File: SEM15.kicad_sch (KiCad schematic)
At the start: 47 parts, among them Q1 PMOS, Q2 PMOS, Q3 PMOS, Q4 PMOS, Q5 PMOS, Q6 PMOS

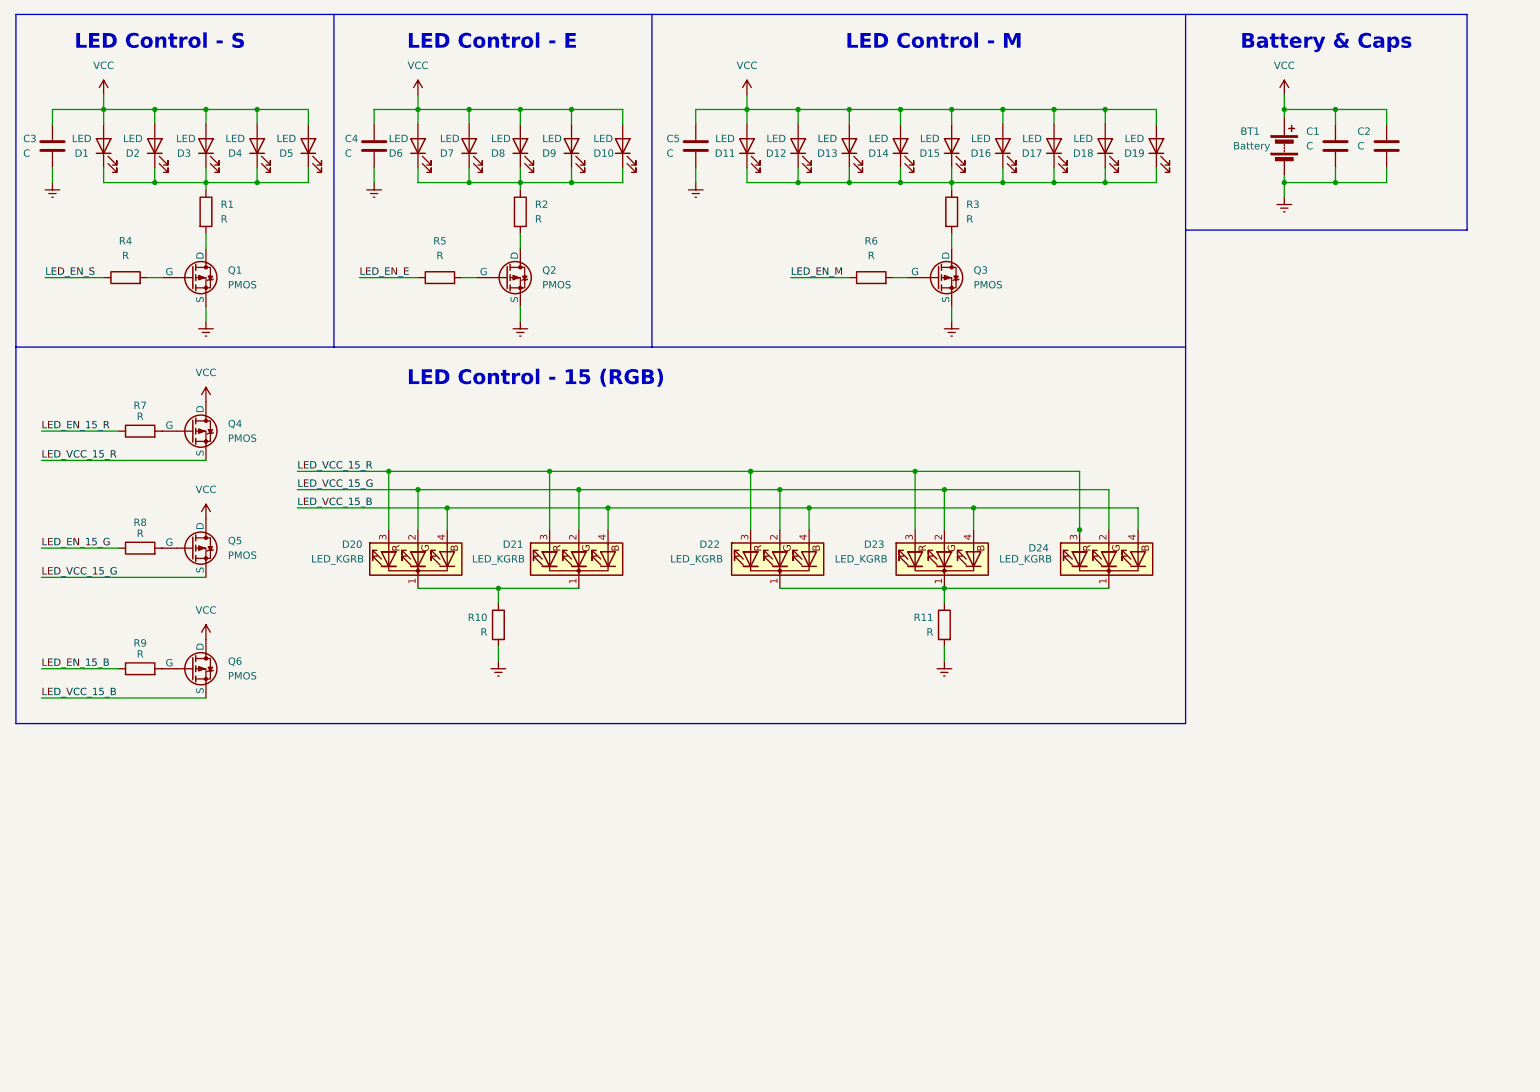
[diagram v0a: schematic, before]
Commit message: rgb es feher led meghajtasa, mikrovezerlo, pcb-n alkatreszrendezgets
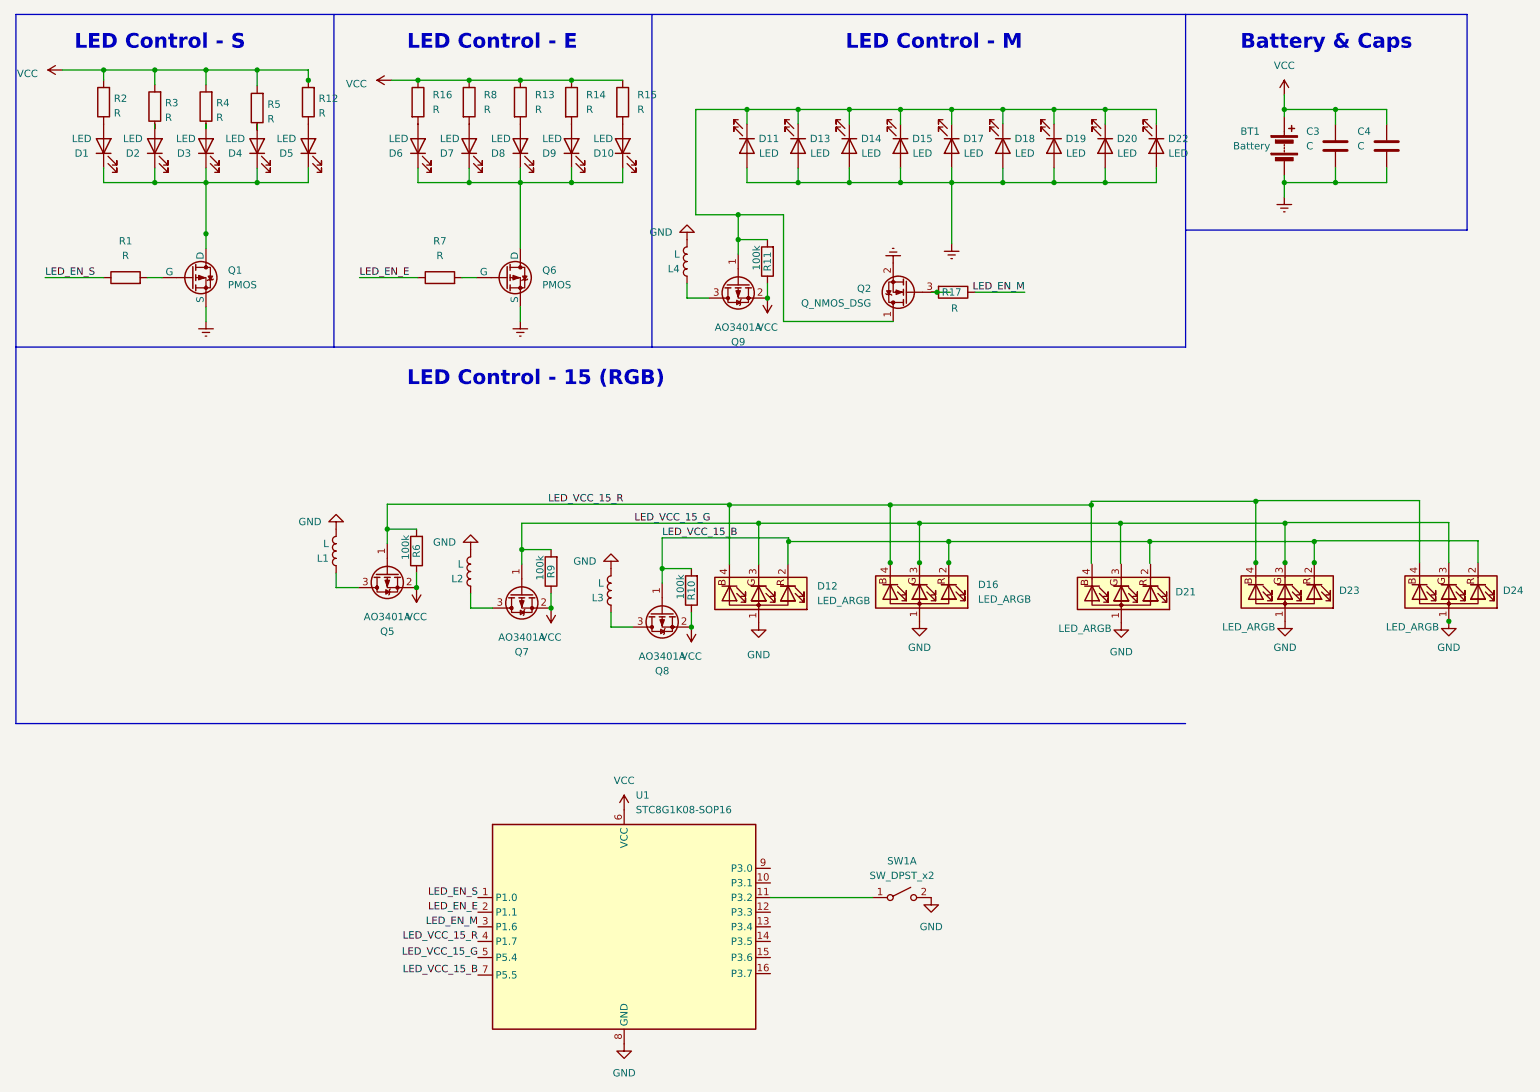
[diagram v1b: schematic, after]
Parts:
- removed C3, C4, C5: C, symbol Device:C
- removed D20, D21, D22, D23, D24: LED_KGRB, LED_SMD:LED_Cree-PLCC4_2x2mm_CW, symbol Device:LED_KGRB
- removed Q3, Q4, Q5, Q6: PMOS, symbol Simulation_SPICE:PMOS
- removed R1, R7: R, symbol Device:R
- added D12, D16, D21, D23, D24: LED_ARGB, LED_SMD:LED_RGB_Wuerth-PLCC4_3.2x2.8mm_150141M173100, symbol Device:LED_ARGB
- added L1, L2, L3, L4: L, Inductor_SMD:L_1008_2520Metric, symbol Device:L
- added Q2: Q_NMOS_DSG, symbol Device:Q_NMOS_DSG
- added Q5, Q7, Q8, Q9: AO3401A, sajat:SOT-23, symbol Transistor_FET:AO3401A
- added R12, R13, R14, R15, R16, R17, R4, R5: R, Resistor_SMD:R_0603_1608Metric, symbol Device:R
- added SW1: SW_DPST_x2, sajat:SW_Push_K2-1102SP, symbol Switch:SW_DPST_x2
- added U1: STC8G1K08-SOP16, Package_SO:STC_SOP-16_3.9x9.9mm_P1.27mm, symbol karifa:STC8G1K08-SOP16
- BT1: footprint (none) -> karifa:CR2032_Holder
- C3: renamed from C1; footprint (none) -> Capacitor_SMD:C_0805_2012Metric
- C4: renamed from C2; footprint (none) -> Capacitor_SMD:C_0805_2012Metric
- R1: renamed from R4; footprint (none) -> Resistor_SMD:R_0603_1608Metric
- R10, R11, R6, R9: value R -> 100k; footprint (none) -> Resistor_SMD:R_0603_1608Metric
- R2, R3, R8: footprint (none) -> Resistor_SMD:R_0603_1608Metric
- R7: renamed from R5; footprint (none) -> Resistor_SMD:R_0603_1608Metric
- renumbered D12 to D13, D13 to D14, D14 to D15, D15 to D17, D16 to D18, D17 to D19, D18 to D20, D19 to D22, Q2 to Q6
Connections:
- net LED_EN_15_B is gone; now on net VCC: R9.1
- net LED_EN_15_G is gone; now on net VCC: R8.1
- net Earth: now also D11.2 (A), D13.2 (A), D14.2 (A), D15.2 (A), D17.2 (A), D18.2 (A), D19.2 (A), D20.2 (A), D22.2 (A), Q2.2 (S); no longer R10.2, R11.2
- net LED_EN_E: now also U1.2 (P1.1)
- net LED_EN_M: now also R17.1, U1.3 (P1.6); no longer R6.1
- net LED_EN_S: now also U1.1 (P1.0)
- net LED_VCC_15_B: now also R10.2, D12.2 (RK), D16.2 (RK), D23.2 (RK), D24.2 (RK), Q8.1 (G), U1.7 (P5.5)
- net LED_VCC_15_G: now also R9.2, D12.3 (GK), D16.3 (GK), D23.3 (GK), D24.3 (GK), Q7.1 (G), U1.5 (P5.4)
- net LED_VCC_15_R: now also R6.2, D12.4 (BK), D16.4 (BK), D23.4 (BK), D24.4 (BK), Q5.1 (G), U1.4 (P1.7)
- net VCC: now also R10.1, R11.1, R2.2, R3.2, R6.1, Q5.2 (S), Q7.2 (S), Q8.2 (S), Q9.2 (S), R12.2, R13.1, R14.1, R15.1, R16.1, R4.2, R5.2, U1.6 (VCC); no longer D1.2 (A), D10.2 (A), D11.2 (A), D13.2 (A), D14.2 (A), D15.2 (A), D17.2 (A), D18.2 (A), D19.2 (A), D2.2 (A), D20.2 (A), D22.2 (A), D3.2 (A), D4.2 (A), D5.2 (A), D6.2 (A), D7.2 (A), D8.2 (A), D9.2 (A)
- net at D11.1 (K), D13.1 (K), D14.1 (K)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: now also R11.2, Q2.1 (D), Q9.1 (G); no longer R3.1
- net at D1.1 (K), D2.1 (K), D3.1 (K)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: now also Q1.1 (D)
- net at D10.1 (K), D6.1 (K), D7.1 (K)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: now also Q6.1 (D); no longer R2.1
- net at R8.2: now also D7.2 (A)
- new net: D10.2 (A), R15.2
- new net: L4.1, Q9.3 (D)
- new net: L1.1, Q5.3 (D)
- new net: D3.2 (A), R4.1
- new net: D1.2 (A), R2.1
- new net: L3.1, Q8.3 (D)
- new net: D4.2 (A), R5.1
- new net: D9.2 (A), R14.2
- new net: SW1.1 (A), U1.11 (P3.2)
- new net: Q2.3 (G), R17.2
- new net: D6.2 (A), R16.2
- new net: L2.1, Q7.3 (D)
- new net: D2.2 (A), R3.1
- new net: D8.2 (A), R13.2
- new net: D5.2 (A), R12.1
- new net GND: D12.1 (A), D16.1 (A), D21.1 (A), D23.1 (A), D24.1 (A), L1.2, L2.2, L3.2, L4.2, SW1.2 (B), U1.8 (GND)
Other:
- moved on the sheet: D11, D13, D14, D15, D17, D18, D19, D20, D22

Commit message: sch kesz
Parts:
- removed D12, D16, D21, D23, D24: LED_ARGB, LED_SMD:LED_RGB_Wuerth-PLCC4_3.2x2.8mm_150141M173100, symbol Device:LED_ARGB
- removed L3: L, Inductor_SMD:L_1008_2520Metric, symbol Device:L
- removed Q1, Q6: PMOS, symbol Simulation_SPICE:PMOS
- removed Q2: Q_NMOS_DSG, symbol Device:Q_NMOS_DSG
- removed Q5, Q7, Q8, Q9: AO3401A, sajat:SOT-23, symbol Transistor_FET:AO3401A
- removed R10: 100k, Resistor_SMD:R_0603_1608Metric, symbol Device:R
- removed R13, R14, R15, R16, R17: R, Resistor_SMD:R_0603_1608Metric, symbol Device:R
- added D12, D16, D21, D25, D26, D27, D28, D29: LED, LED_SMD:LED_0805_2012Metric, symbol Device:LED
- added J1: Conn_01x04, Connector_PinHeader_1.27mm:PinHeader_1x04_P1.27mm_Vertical, symbol Connector_Generic:Conn_01x04
- added L5: L, Inductor_SMD:L_1008_2520Metric, symbol Device:L
- added Q1, Q2, Q3, Q4: AO3401A, sajat:SOT-23, symbol Transistor_FET:AO3401A
- R1: value R -> 100k
- R12, R4, R5, R7, R8: footprint Resistor_SMD:R_0603_1608Metric -> (none)
- R2: value R -> 510; footprint Resistor_SMD:R_0603_1608Metric -> (none)
- R3: value R -> 1k; footprint Resistor_SMD:R_0603_1608Metric -> (none)
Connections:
- net Earth: now also D1.2 (A), D10.2 (A), D2.2 (A), D3.2 (A), D4.2 (A), D5.2 (A), D6.2 (A), D7.2 (A), D8.2 (A), D9.2 (A), D25.2 (A), D26.2 (A), D27.2 (A), D28.2 (A), D29.2 (A); no longer D11.2 (A), D13.2 (A), D14.2 (A), D15.2 (A), D17.2 (A), D18.2 (A), D19.2 (A), D20.2 (A), D22.2 (A)
- net GND: now also J1.4 (Pin_4), L5.2
- net LED_EN_E: now also R1.2, Q2.1 (G); no longer R7.1
- net LED_EN_M: no longer U1.3 (P1.6)
- net LED_EN_S: now also R11.2, Q1.1 (G); no longer R1.1
- net VCC: now also R1.1, R7.2, R8.2, J1.1 (Pin_1), Q1.2 (S), Q2.2 (S), Q3.2 (S), Q4.2 (S); no longer R8.1
- net at L4.1: now also D1.1 (K), D2.1 (K), D3.1 (K), D4.1 (K), D5.1 (K), Q1.3 (D)
- net at L1.1: now also D12.1 (K), D16.1 (K), D21.1 (K), Q3.3 (D)
- net at R4.1: now also D15.2 (A); no longer D3.2 (A)
- net at R2.1: now also D11.2 (A), D13.2 (A); no longer D1.2 (A)
- net at R5.1: now also D17.2 (A); no longer D4.2 (A)
- net P3.1: now reaches U1.10 (P3.1)
- net P3.1: now also J1.3 (Pin_3)
- net LED_EN_M5: now reaches U1.12 (P3.3)
- net LED_EN_M5: now also D18.1 (K)
- net LED_EN_M6: now reaches U1.13 (P3.4)
- net LED_EN_M6: now also D19.1 (K)
- net LED_EN_M7: now reaches U1.14 (P3.5)
- net LED_EN_M7: now also D20.1 (K), D22.1 (K)
- net LED_EN_1: now reaches U1.15 (P3.6)
- net LED_EN_1: now also R6.2, Q3.1 (G)
- net LED_EN_5: now reaches U1.16 (P3.7)
- net LED_EN_5: now also R9.2, Q4.1 (G)
- net P3.0: now reaches U1.9 (P3.0)
- net P3.0: now also J1.2 (Pin_2)
- net at L2.1: now also D25.1 (K), D26.1 (K), D27.1 (K), D28.1 (K), D29.1 (K), Q4.3 (D)
- net at R3.1: now also D14.2 (A); no longer D2.2 (A)
- net at R12.1: now also D20.2 (A), D22.2 (A); no longer D5.2 (A)
- net LED_VCC_15_B renamed LED_EN_M4
- net LED_EN_M4: now also D17.1 (K)
- net LED_VCC_15_G renamed LED_EN_M3
- net LED_EN_M3: now also D15.1 (K); no longer R9.2
- net LED_VCC_15_R renamed LED_EN_M2
- net LED_EN_M2: now also D14.1 (K); no longer R6.2
- new net: L5.1, Q2.3 (D)
- new net: D18.2 (A), R7.1
- new net: D19.2 (A), R8.1
- new net: D12.2 (A), D16.2 (A), D21.2 (A)
- new net LED_EN_M1: D11.1 (K), D13.1 (K), U1.3 (P1.6)
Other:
- moved on the sheet: D1, D10, D2, D3, D4, D5, D6, D7, D8, D9

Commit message: pcb nagyreszt
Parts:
- removed D16: LED, LED_SMD:LED_0805_2012Metric, symbol Device:LED
- added D23, D24: LED, LED_SMD:LED_0805_2012Metric, symbol Device:LED
- R12, R2, R3, R5, R7, R8: footprint (none) -> Resistor_SMD:R_0603_1608Metric
- R4: value R -> 510; footprint (none) -> Resistor_SMD:R_0603_1608Metric
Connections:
- net Earth is gone; now on net GND: BT1.2 (-), C3.2, C4.2, D1.2 (A), D10.2 (A), D2.2 (A), D25.2 (A), D26.2 (A), D27.2 (A), D28.2 (A), D29.2 (A), D3.2 (A), D4.2 (A), D5.2 (A), D6.2 (A), D7.2 (A), D8.2 (A), D9.2 (A)
- net GND: now also D12.2 (A), D21.2 (A)
- net LED_EN_1: now also U1.16 (P3.7); no longer U1.15 (P3.6)
- net LED_EN_5: now also U1.12 (P3.3); no longer U1.16 (P3.7)
- net LED_EN_E: now also U1.5 (P5.4); no longer U1.2 (P1.1)
- net LED_EN_M1: now also U1.4 (P1.7); no longer U1.3 (P1.6)
- net LED_EN_M2: now also U1.3 (P1.6); no longer U1.4 (P1.7)
- net LED_EN_M3: now also U1.2 (P1.1), D23.1 (K); no longer D15.1 (K), U1.5 (P5.4)
- net LED_EN_M4: now also D15.1 (K), U1.1 (P1.0), D24.1 (K); no longer D17.1 (K), U1.7 (P5.5)
- net LED_EN_M5: now also D17.1 (K), U1.14 (P3.5); no longer D18.1 (K), U1.12 (P3.3)
- net LED_EN_M6: now also D18.1 (K)
- net LED_EN_M7: now also U1.11 (P3.2); no longer U1.14 (P3.5)
- net LED_EN_S: now also U1.7 (P5.5); no longer U1.1 (P1.0)
- net at L5.1, Q2.3 (D): now also D10.1 (K), D6.1 (K), D7.1 (K), D8.1 (K), D9.1 (K)
- net SW_IN: now reaches SW1.1 (A)
- net SW_IN: now also U1.15 (P3.6); no longer U1.11 (P3.2)
- net at D18.2 (A), R7.1: now also D19.2 (A)
- net at R8.1: now also D23.2 (A); no longer D19.2 (A)
- net at D15.2 (A), R4.1: now also D24.2 (A)
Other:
- note added: "LED Control - 15 (White)"
- note removed: "LED Control - 15 (RGB)"
- moved on the sheet: D11, D13, D14, D15, R2, R3, R4

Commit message: rogzitok
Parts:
- added J2, J3, J4, J5, J6, J7, J8, J9: Conn_01x01_Male, Connector_PinHeader_2.54mm:PinHeader_1x01_P2.54mm_Vertical, symbol Connector:Conn_01x01_Male
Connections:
- net GND: now also J2.1 (Pin_1), J3.1 (Pin_1), J4.1 (Pin_1), J5.1 (Pin_1), J6.1 (Pin_1), J7.1 (Pin_1), J8.1 (Pin_1), J9.1 (Pin_1)

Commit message: BOM terv
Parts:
- C3: value C -> 100n
- C4: value C -> 10u
- R12, R7: value R -> 510
- R5, R8: value R -> 1k
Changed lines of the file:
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@@
       (effects (font (size 1.27 1.27)) (justify left))
     )
-    (property "Value" "R" (at 187.96 46.863 0)
+    (property "Value" "510" (at 187.96 46.863 0)
       (effects (font (size 1.27 1.27)) (justify left))
     )
@@
       (effects (font (size 1.27 1.27)) (justify left))
     )
-    (property "Value" "R" (at 153.416 44.069 0)
+    (property "Value" "1k" (at 153.416 44.069 0)
       (effects (font (size 1.27 1.27)) (justify left))
     )
@@
       (effects (font (size 1.27 1.27)) (justify left))
     )
-    (property "Value" "C" (at 247.015 36.83 0)
+    (property "Value" "10u" (at 247.015 36.83 0)
       (effects (font (size 1.27 1.27)) (justify left))
     )
@@
       (effects (font (size 1.27 1.27)) (justify left))
     )
-    (property "Value" "C" (at 238.125 36.83 0)
+    (property "Value" "100n" (at 238.125 36.83 0)
       (effects (font (size 1.27 1.27)) (justify left))
     )
@@
       (effects (font (size 1.27 1.27)) (justify left))
     )
-    (property "Value" "R" (at 205.74 52.451 0)
+    (property "Value" "510" (at 205.74 52.451 0)
       (effects (font (size 1.27 1.27)) (justify left))
     )
@@
       (effects (font (size 1.27 1.27)) (justify left))
     )
-    (property "Value" "R" (at 179.07 46.863 0)
-      (effects (font (size 1.27 1.27)) (justify left))
-    )
+    (property "Value" "1k" (at 179.07 46.863 0)
+      (effects (font (size 1.27 1.27)) (justify left))
+    )

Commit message: uj gomb, kivagas
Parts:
- removed J8, J9: Conn_01x01_Male, Connector_PinHeader_2.54mm:PinHeader_1x01_P2.54mm_Vertical, symbol Connector:Conn_01x01_Male
- SW1: footprint sajat:SW_Push_K2-1102SP -> sajat:magasgomb
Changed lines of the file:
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@@
-    )
-  )
-  (symbol (lib_id "Connector:Conn_01x01_Male") (at 207.518 128.524 180) (unit 1)
-    (in_bom yes) (on_board yes) (dnp no) (fields_autoplaced)
-    (property "Reference" "J9" (at 206.883 123.952 0)
-      (effects (font (size 1.27 1.27)))
-    )
-    (property "Value" "Conn_01x01_Male" (at 206.883 126.492 0)
-      (effects (font (size 1.27 1.27)))
-    )
-    (property "Footprint" "Connector_PinHeader_2.54mm:PinHeader_1x01_P2.54mm_Vertical" (at 207.518 128.524 0)
-      (effects (font (size 1.27 1.27)) hide)
-    )
-    (property "Datasheet" "~" (at 207.518 128.524 0)
-      (effects (font (size 1.27 1.27)) hide)
-    )
-    (pin "1")
-    (instances
-      (project "SEM15"
-        (path "/0fdb131f-7535-4030-b35f-e7b26b07455b"
-          (reference "J9") (unit 1)
-        )
-      )
     )
   )
@@
       (effects (font (size 1.27 1.27)))
     )
-    (property "Footprint" "sajat:SW_Push_K2-1102SP" (at 167.894 167.386 0)
+    (property "Footprint" "sajat:magasgomb" (at 167.894 167.386 0)
       (effects (font (size 1.27 1.27)) hide)
     )
@@
     )
   )
-  (symbol (lib_id "power:GND") (at 202.438 128.524 270) (unit 1)
-    (in_bom yes) (on_board yes) (dnp no) (fields_autoplaced)
-    (property "Reference" "#PWR034" (at 196.088 128.524 0)
-      (effects (font (size 1.27 1.27)) hide)
-    )
-    (property "Value" "GND" (at 198.374 129.159 90)
-      (effects (font (size 1.27 1.27)) (justify right))
-    )
-    (property "Footprint" "" (at 202.438 128.524 0)
-      (effects (font (size 1.27 1.27)) hide)
-    )
-    (property "Datasheet" "" (at 202.438 128.524 0)
-      (effects (font (size 1.27 1.27)) hide)
-    )
-    (pin "1")
-    (instances
-      (project "SEM15"
-        (path "/0fdb131f-7535-4030-b35f-e7b26b07455b"
-          (reference "#PWR034") (unit 1)
-        )
-      )
-      (project "karifa"
-        (path "/30f28fd8-ef05-4208-b612-7ffefcdba2ba"
-          (reference "#PWR?") (unit 1)
-        )
-      )
-    )
-  )
   (symbol (lib_id "Device:LED") (at 168.148 37.338 270) (unit 1)
     (in_bom yes) (on_board yes) (dnp no)
@@
     )
   )
-  (symbol (lib_id "power:GND") (at 202.184 124.968 270) (unit 1)
-    (in_bom yes) (on_board yes) (dnp no) (fields_autoplaced)
-    (property "Reference" "#PWR033" (at 195.834 124.968 0)
-      (effects (font (size 1.27 1.27)) hide)
-    )
-    (property "Value" "GND" (at 198.12 125.603 90)
-      (effects (font (size 1.27 1.27)) (justify right))
-    )
-    (property "Footprint" "" (at 202.184 124.968 0)
-      (effects (font (size 1.27 1.27)) hide)
-    )
-    (property "Datasheet" "" (at 202.184 124.968 0)
-      (effects (font (size 1.27 1.27)) hide)
-    )
-    (pin "1")
-    (instances
-      (project "SEM15"
-        (path "/0fdb131f-7535-4030-b35f-e7b26b07455b"
-          (reference "#PWR033") (unit 1)
-        )
-      )
-      (project "karifa"
-        (path "/30f28fd8-ef05-4208-b612-7ffefcdba2ba"
-          (reference "#PWR?") (unit 1)
-        )
-      )
-    )
-  )
   (symbol (lib_id "Connector:Conn_01x01_Male") (at 208.026 108.204 180) (unit 1)
     (in_bom yes) (on_board yes) (dnp no) (fields_autoplaced)
@@
         )
       )
-    )
-  )
-  (symbol (lib_id "Connector:Conn_01x01_Male") (at 207.264 124.968 180) (unit 1)
-    (in_bom yes) (on_board yes) (dnp no) (fields_autoplaced)
-    (property "Reference" "J8" (at 206.629 120.396 0)
-      (effects (font (size 1.27 1.27)))
-    )
-    (property "Value" "Conn_01x01_Male" (at 206.629 122.936 0)
-      (effects (font (size 1.27 1.27)))
-    )
-    (property "Footprint" "Connector_PinHeader_2.54mm:PinHeader_1x01_P2.54mm_Vertical" (at 207.264 124.968 0)
-      (effects (font (size 1.27 1.27)) hide)
-    )
-    (property "Datasheet" "~" (at 207.264 124.968 0)
-      (effects (font (size 1.27 1.27)) hide)
-    )
-    (pin "1")
-    (instances
-      (project "SEM15"
-        (path "/0fdb131f-7535-4030-b35f-e7b26b07455b"
-          (reference "J8") (unit 1)
-        )
-      )

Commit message: gerberek, bom
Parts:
- added T1: Tab, kikit:Tab, symbol kikit:Tab
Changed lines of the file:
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@@
+    )
+  )
+  (symbol (lib_id "kikit:Tab") (at 101.092 103.886 0) (unit 1)
+    (in_bom no) (on_board yes) (dnp no) (fields_autoplaced)
+    (property "Reference" "T1" (at 106.172 101.9809 0)
+      (effects (font (size 1.27 1.27)) (justify left))
+    )
+    (property "Value" "Tab" (at 106.172 104.5209 0)
+      (effects (font (size 1.27 1.27)) (justify left))
+    )
+    (property "Footprint" "kikit:Tab" (at 101.092 103.886 0)
+      (effects (font (size 1.27 1.27)) hide)
+    )
+    (property "Datasheet" "" (at 101.092 103.886 0)
+      (effects (font (size 1.27 1.27)) hide)
+    )
+    (instances
+      (project "SEM15"
+        (path "/0fdb131f-7535-4030-b35f-e7b26b07455b"
+          (reference "T1") (unit 1)
+        )
+      )
+      (project "karifa"
+        (path "/30f28fd8-ef05-4208-b612-7ffefcdba2ba"
+          (reference "T1") (unit 1)
+        )
+      )
     )
   )
